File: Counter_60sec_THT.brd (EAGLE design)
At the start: 90 x 75 mm, 39 parts, among them IC1 74LS90N, IC10 7805T, IC2 74LS90N, IC3 74LS48N, IC4 74LS48N, IC5 74ALS08N, IC6 LM555N, IC7 74LS14N, IC8 7476N, IC9 74LS32N

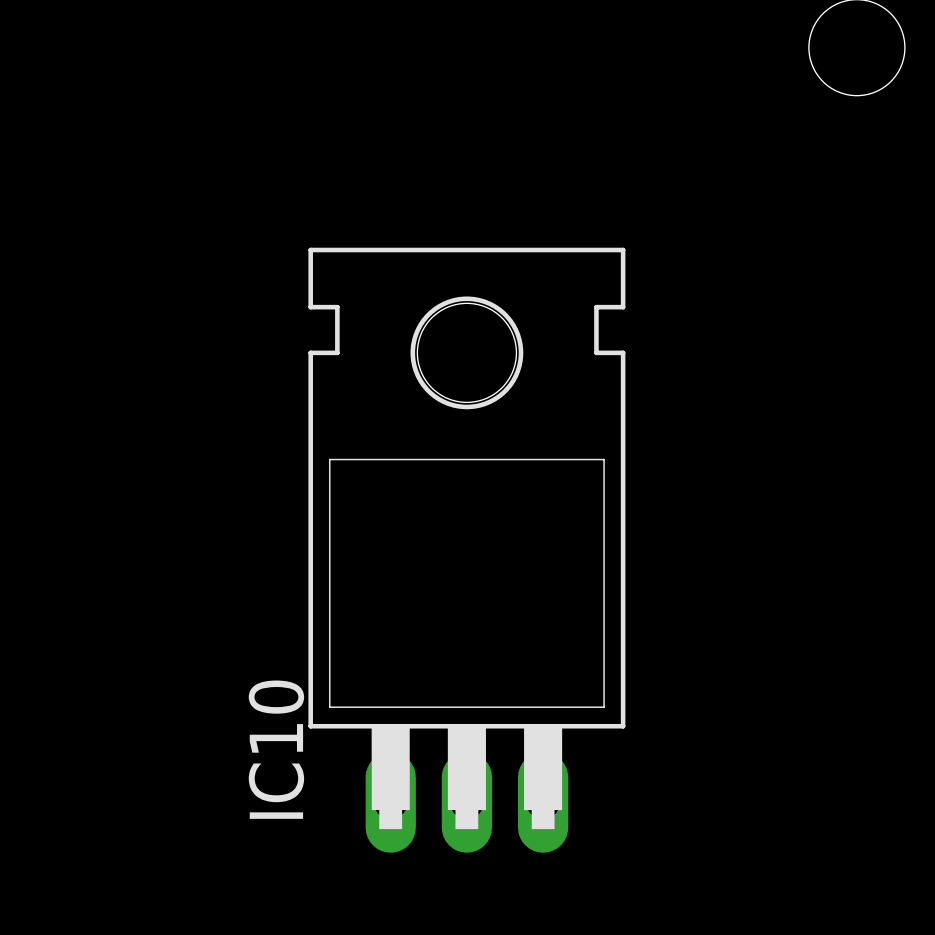
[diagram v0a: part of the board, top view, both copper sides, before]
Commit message: [Zach] Added heatsink
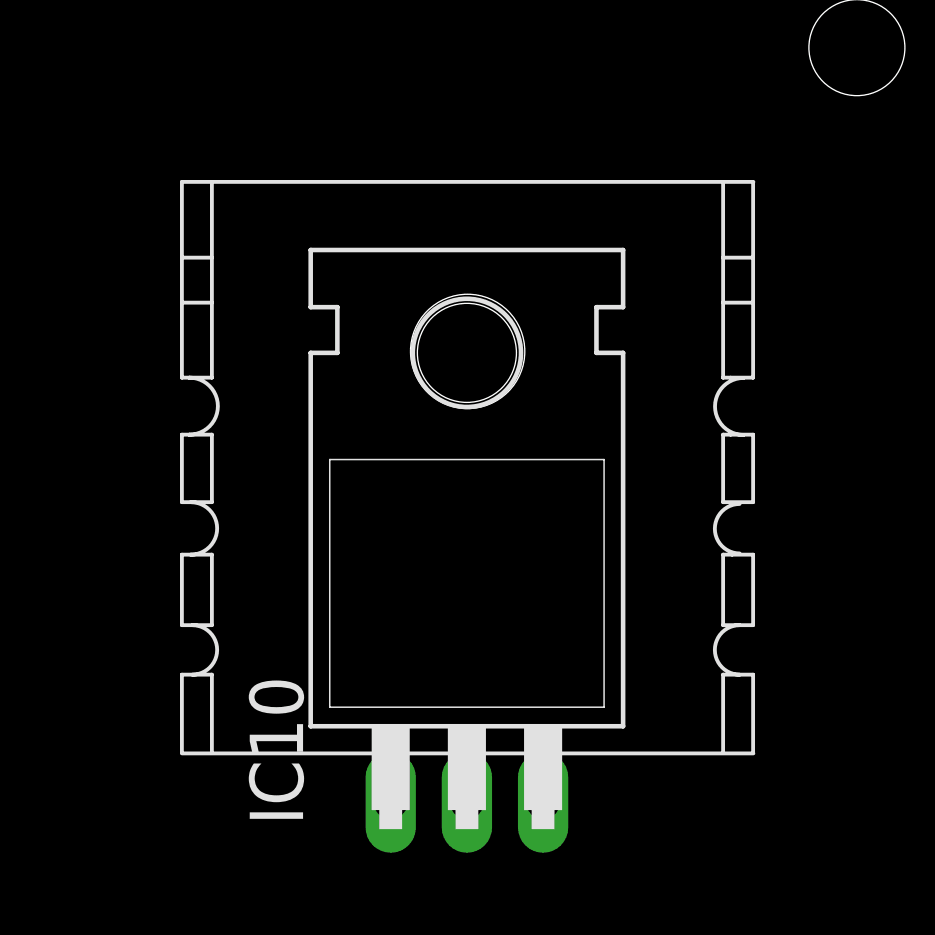
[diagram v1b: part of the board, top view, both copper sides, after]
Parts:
- added HS1: 507302B00000G, to220-heatsink:TO-220H
